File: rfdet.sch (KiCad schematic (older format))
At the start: 6 parts

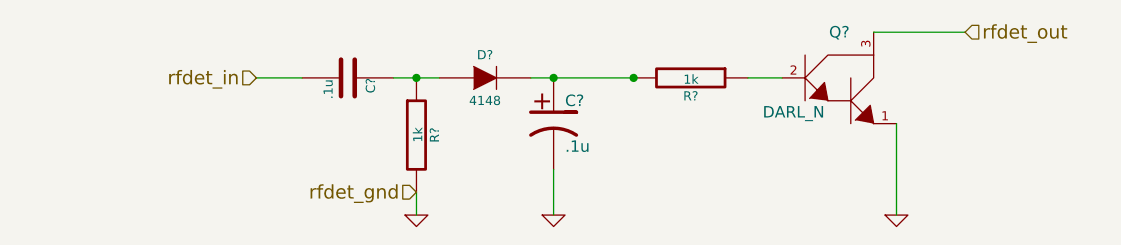
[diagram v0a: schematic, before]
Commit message: Finished/annotated rfdet schematic
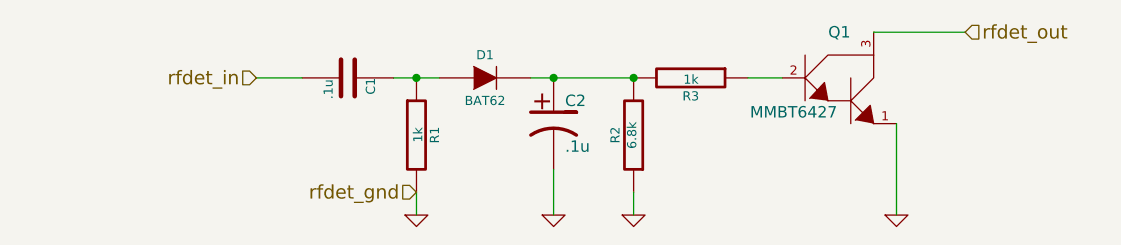
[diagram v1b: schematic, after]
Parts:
- added R2: 6.8k, symbol R
- D1: renamed from D?; value 4148 -> BAT62
- Q1: renamed from Q?; value DARL_N -> MMBT6427
- gave numbers to parts that had none: 4
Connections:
- net GND: now also R2.1
- net at C2.1, D1.2 (K), R3.2: now also R2.2
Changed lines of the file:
@@
 LIBS:contrib
 LIBS:valves
-LIBS:transfo-dots
 LIBS:mcus
+LIBS:transformers
 LIBS:qrpamp-cache
 EELAYER 24 0
@@
 $EndDescr
 $Comp
-L C C?
+L C C1
 U 1 1 5470CFC5
 P 4800 3700
-F 0 "C?" H 4800 3800 40  0000 L CNN
+F 0 "C1" H 4800 3800 40  0000 L CNN
 F 1 ".1u" H 4806 3615 40  0000 L CNN
 F 2 "" H 4838 3550 30  0000 C CNN
@@
 $EndComp
 $Comp
-L DIODE D?
+L DIODE D1
 U 1 1 5470CFD9
 P 5400 3700
-F 0 "D?" H 5400 3800 40  0000 C CNN
-F 1 "4148" H 5400 3600 40  0000 C CNN
+F 0 "D1" H 5400 3800 40  0000 C CNN
+F 1 "BAT62" H 5400 3600 40  0000 C CNN
 F 2 "" H 5400 3700 60  0000 C CNN
 F 3 "" H 5400 3700 60  0000 C CNN
@@
 $EndComp
 $Comp
-L CP1 C?
+L CP1 C2
 U 1 1 5470CFED
 P 5700 3900
-F 0 "C?" H 5750 4000 50  0000 L CNN
+F 0 "C2" H 5750 4000 50  0000 L CNN
 F 1 ".1u" H 5750 3800 50  0000 L CNN
 F 2 "" H 5700 3900 60  0000 C CNN
@@
 $EndComp
 $Comp
-L R R?
+L R R3
 U 1 1 5470D001
 P 6300 3700
-F 0 "R?" V 6380 3700 40  0000 C CNN
+F 0 "R3" V 6380 3700 40  0000 C CNN
 F 1 "1k" V 6307 3701 40  0000 C CNN
 F 2 "" V 6230 3700 30  0000 C CNN
@@
 $EndComp
 $Comp
-L R R?
+L R R1
 U 1 1 5470D02C
 P 5100 3950
-F 0 "R?" V 5180 3950 40  0000 C CNN
+F 0 "R1" V 5180 3950 40  0000 C CNN
 F 1 "1k" V 5107 3951 40  0000 C CNN
 F 2 "" V 5030 3950 30  0000 C CNN
@@
 $EndComp
 $Comp
-L GND #PWR?
+L GND #PWR2
 U 1 1 5470D04B
 P 5700 4300
-F 0 "#PWR?" H 5700 4300 30  0001 C CNN
+F 0 "#PWR2" H 5700 4300 30  0001 C CNN
 F 1 "GND" H 5700 4230 30  0001 C CNN
 F 2 "" H 5700 4300 60  0000 C CNN
@@
 $EndComp
 $Comp
-L GND #PWR?
+L GND #PWR1
 U 1 1 5470D056
 P 5100 4300
-F 0 "#PWR?" H 5100 4300 30  0001 C CNN
+F 0 "#PWR1" H 5100 4300 30  0001 C CNN
 F 1 "GND" H 5100 4230 30  0001 C CNN
 F 2 "" H 5100 4300 60  0000 C CNN
@@
 	4600 3700 4400 3700
 $Comp
-L DARL_N Q?
+L DARL_N Q1
 U 1 1 5470D157
 P 6950 3750
-F 0 "Q?" H 6950 4000 50  0000 C CNN
-F 1 "DARL_N" H 6750 3650 50  0000 C CNN
+F 0 "Q1" H 6950 4000 50  0000 C CNN
+F 1 "MMBT6427" H 6750 3650 50  0000 C CNN
 F 2 "" H 6950 3750 60  0000 C CNN
 F 3 "" H 6950 3750 60  0000 C CNN
@@
 	6550 3700 6700 3700
 $Comp
-L GND #PWR?
+L GND #PWR4
 U 1 1 5470D254
 P 7200 4300
-F 0 "#PWR?" H 7200 4300 30  0001 C CNN
+F 0 "#PWR4" H 7200 4300 30  0001 C CNN
 F 1 "GND" H 7200 4230 30  0001 C CNN
 F 2 "" H 7200 4300 60  0000 C CNN
@@
 Text HLabel 5100 4200 0    60   Input ~ 0
 rfdet_gnd
+$Comp
+L R R2
+U 1 1 5477B801
+P 6050 3950
+F 0 "R2" V 6130 3950 40  0000 C CNN
+F 1 "6.8k" V 6057 3951 40  0000 C CNN
+F 2 "" V 5980 3950 30  0000 C CNN
+F 3 "" H 6050 3950 30  0000 C CNN
+	1    6050 3950
+	-1   0    0    1
+$EndComp
+$Comp
+L GND #PWR3
+U 1 1 5477B80C
+P 6050 4300
+F 0 "#PWR3" H 6050 4300 30  0001 C CNN
+F 1 "GND" H 6050 4230 30  0001 C CNN
+F 2 "" H 6050 4300 60  0000 C CNN
+F 3 "" H 6050 4300 60  0000 C CNN
+	1    6050 4300
+	1    0    0    -1
+$EndComp
+Wire Wire Line
+	6050 4200 6050 4300
 $EndSCHEMATC

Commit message: Added simulation dir
Also, due to simulation, modified the rf detector circuit
to have higher input impdedance to distort the input rf
less.
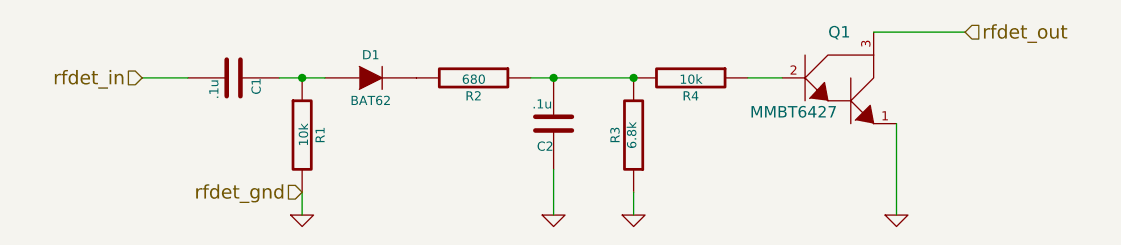
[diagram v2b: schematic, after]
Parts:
- removed C2: .1u, symbol CP1
- added C2: .1u, symbol C
- added R2: 680, symbol R
- R1: value 1k -> 10k
- R4: renamed from R3; value 1k -> 10k
- renumbered R2 to R3
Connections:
- net GND: now also C2.1
- net at R3.2, R4.2: now also C2.2, R2.1; no longer D1.2 (K)
- new net: D1.2 (K), R2.2
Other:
- moved on the sheet: C1, D1, R1
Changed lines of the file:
@@
 L C C1
 U 1 1 5470CFC5
-P 4800 3700
-F 0 "C1" H 4800 3800 40  0000 L CNN
-F 1 ".1u" H 4806 3615 40  0000 L CNN
-F 2 "" H 4838 3550 30  0000 C CNN
-F 3 "" H 4800 3700 60  0000 C CNN
-	1    4800 3700
+P 4300 3700
+F 0 "C1" H 4300 3800 40  0000 L CNN
+F 1 ".1u" H 4306 3615 40  0000 L CNN
+F 2 "" H 4338 3550 30  0000 C CNN
+F 3 "" H 4300 3700 60  0000 C CNN
+	1    4300 3700
 	0    1    1    0
 $EndComp
@@
 L DIODE D1
 U 1 1 5470CFD9
-P 5400 3700
-F 0 "D1" H 5400 3800 40  0000 C CNN
-F 1 "BAT62" H 5400 3600 40  0000 C CNN
-F 2 "" H 5400 3700 60  0000 C CNN
-F 3 "" H 5400 3700 60  0000 C CNN
-	1    5400 3700
+P 4900 3700
+F 0 "D1" H 4900 3800 40  0000 C CNN
+F 1 "BAT62" H 4900 3600 40  0000 C CNN
+F 2 "" H 4900 3700 60  0000 C CNN
+F 3 "" H 4900 3700 60  0000 C CNN
+	1    4900 3700
 	1    0    0    -1
 $EndComp
 $Comp
-L CP1 C2
-U 1 1 5470CFED
-P 5700 3900
-F 0 "C2" H 5750 4000 50  0000 L CNN
-F 1 ".1u" H 5750 3800 50  0000 L CNN
-F 2 "" H 5700 3900 60  0000 C CNN
-F 3 "" H 5700 3900 60  0000 C CNN
-	1    5700 3900
-	1    0    0    -1
-$EndComp
-$Comp
-L R R3
+L R R4
 U 1 1 5470D001
 P 6300 3700
-F 0 "R3" V 6380 3700 40  0000 C CNN
-F 1 "1k" V 6307 3701 40  0000 C CNN
+F 0 "R4" V 6380 3700 40  0000 C CNN
+F 1 "10k" V 6307 3701 40  0000 C CNN
 F 2 "" V 6230 3700 30  0000 C CNN
 F 3 "" H 6300 3700 30  0000 C CNN
@@
 L R R1
 U 1 1 5470D02C
-P 5100 3950
-F 0 "R1" V 5180 3950 40  0000 C CNN
-F 1 "1k" V 5107 3951 40  0000 C CNN
-F 2 "" V 5030 3950 30  0000 C CNN
-F 3 "" H 5100 3950 30  0000 C CNN
-	1    5100 3950
+P 4600 3950
+F 0 "R1" V 4680 3950 40  0000 C CNN
+F 1 "10k" V 4607 3951 40  0000 C CNN
+F 2 "" V 4530 3950 30  0000 C CNN
+F 3 "" H 4600 3950 30  0000 C CNN
+	1    4600 3950
 	1    0    0    -1
 $EndComp
@@
 L GND #PWR1
 U 1 1 5470D056
-P 5100 4300
-F 0 "#PWR1" H 5100 4300 30  0001 C CNN
-F 1 "GND" H 5100 4230 30  0001 C CNN
-F 2 "" H 5100 4300 60  0000 C CNN
-F 3 "" H 5100 4300 60  0000 C CNN
-	1    5100 4300
+P 4600 4300
+F 0 "#PWR1" H 4600 4300 30  0001 C CNN
+F 1 "GND" H 4600 4230 30  0001 C CNN
+F 2 "" H 4600 4300 60  0000 C CNN
+F 3 "" H 4600 4300 60  0000 C CNN
+	1    4600 4300
 	1    0    0    -1
 $EndComp
 Wire Wire Line
-	5000 3700 5200 3700
-Connection ~ 5100 3700
+	4500 3700 4700 3700
+Connection ~ 4600 3700
 Connection ~ 5700 3700
 Connection ~ 6050 3700
@@
 	5700 4100 5700 4300
 Wire Wire Line
-	5100 4200 5100 4300
+	4600 4200 4600 4300
 Wire Wire Line
-	4600 3700 4400 3700
+	4100 3700 3900 3700
 $Comp
 L DARL_N Q1
@@
 Text HLabel 7500 3500 2    60   Input ~ 0
 rfdet_out
-Text HLabel 4400 3700 0    60   Input ~ 0
+Text HLabel 3900 3700 0    60   Input ~ 0
 rfdet_in
-Text HLabel 5100 4200 0    60   Input ~ 0
+Text HLabel 4600 4200 0    60   Input ~ 0
 rfdet_gnd
 $Comp
-L R R2
+L R R3
 U 1 1 5477B801
 P 6050 3950
-F 0 "R2" V 6130 3950 40  0000 C CNN
+F 0 "R3" V 6130 3950 40  0000 C CNN
 F 1 "6.8k" V 6057 3951 40  0000 C CNN
 F 2 "" V 5980 3950 30  0000 C CNN
@@
 Wire Wire Line
 	6050 4200 6050 4300
+$Comp
+L R R2
+U 1 1 54788FD0
+P 5350 3700
+F 0 "R2" V 5430 3700 40  0000 C CNN
+F 1 "680" V 5357 3701 40  0000 C CNN
+F 2 "" V 5280 3700 30  0000 C CNN
+F 3 "" H 5350 3700 30  0000 C CNN
+	1    5350 3700
+	0    1    1    0
+$EndComp
+$Comp
+L C C2
+U 1 1 54788FE2
+P 5700 3900
+F 0 "C2" H 5700 4000 40  0000 L CNN
+F 1 ".1u" H 5706 3815 40  0000 L CNN
+F 2 "" H 5738 3750 30  0000 C CNN
+F 3 "" H 5700 3900 60  0000 C CNN
+	1    5700 3900
+	-1   0    0    1
+$EndComp
 $EndSCHEMATC

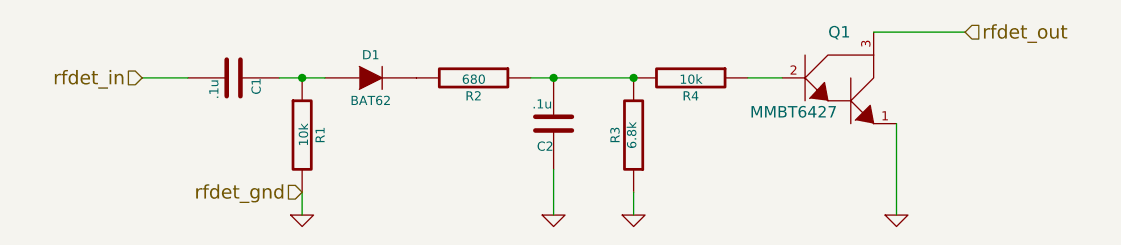
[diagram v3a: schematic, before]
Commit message: Associate more footprints
- Removed flyback diodes from amp
- Changed BAT62 -> SD101 (BAT62 is EOL)
- Changed R and C footprints for hand-soldered versions
- Associated through-hole cap footprints
- Associated regulator footprints
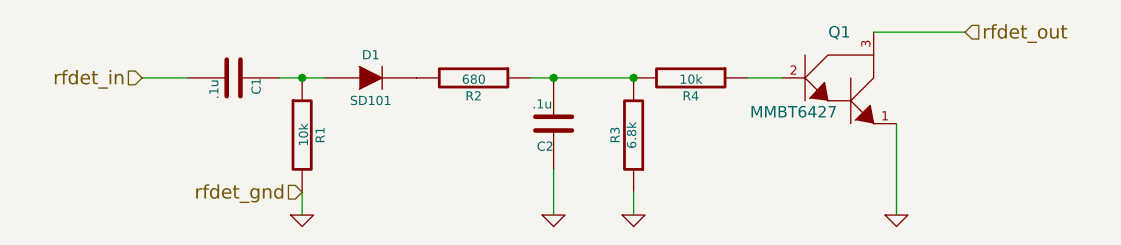
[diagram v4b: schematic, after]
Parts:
- C1, C2: footprint (none) -> Capacitors_SMD:C_0805_HandSoldering
- D1: value BAT62 -> SD101
- R1, R2, R3, R4: footprint (none) -> Resistors_SMD:R_1206_HandSoldering
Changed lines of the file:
@@
 LIBS:transformers
 LIBS:qrpamp-cache
-EELAYER 24 0
+EELAYER 25 0
 EELAYER END
 $Descr A4 11693 8268
@@
 F 0 "C1" H 4300 3800 40  0000 L CNN
 F 1 ".1u" H 4306 3615 40  0000 L CNN
-F 2 "" H 4338 3550 30  0000 C CNN
+F 2 "Capacitors_SMD:C_0805_HandSoldering" H 4338 3550 30  0001 C CNN
 F 3 "" H 4300 3700 60  0000 C CNN
 	1    4300 3700
@@
 P 4900 3700
 F 0 "D1" H 4900 3800 40  0000 C CNN
-F 1 "BAT62" H 4900 3600 40  0000 C CNN
-F 2 "" H 4900 3700 60  0000 C CNN
+F 1 "SD101" H 4900 3600 40  0000 C CNN
+F 2 "" H 4900 3700 60  0001 C CNN
 F 3 "" H 4900 3700 60  0000 C CNN
 	1    4900 3700
@@
 F 0 "R4" V 6380 3700 40  0000 C CNN
 F 1 "10k" V 6307 3701 40  0000 C CNN
-F 2 "" V 6230 3700 30  0000 C CNN
+F 2 "Resistors_SMD:R_1206_HandSoldering" V 6230 3700 30  0001 C CNN
 F 3 "" H 6300 3700 30  0000 C CNN
 	1    6300 3700
@@
 F 0 "R1" V 4680 3950 40  0000 C CNN
 F 1 "10k" V 4607 3951 40  0000 C CNN
-F 2 "" V 4530 3950 30  0000 C CNN
+F 2 "Resistors_SMD:R_1206_HandSoldering" V 4530 3950 30  0001 C CNN
 F 3 "" H 4600 3950 30  0000 C CNN
 	1    4600 3950
@@
 F 0 "Q1" H 6950 4000 50  0000 C CNN
 F 1 "MMBT6427" H 6750 3650 50  0000 C CNN
-F 2 "" H 6950 3750 60  0000 C CNN
+F 2 "" H 6950 3750 60  0001 C CNN
 F 3 "" H 6950 3750 60  0000 C CNN
 	1    6950 3750
@@
 F 0 "R3" V 6130 3950 40  0000 C CNN
 F 1 "6.8k" V 6057 3951 40  0000 C CNN
-F 2 "" V 5980 3950 30  0000 C CNN
+F 2 "Resistors_SMD:R_1206_HandSoldering" V 5980 3950 30  0001 C CNN
 F 3 "" H 6050 3950 30  0000 C CNN
 	1    6050 3950
@@
 F 0 "R2" V 5430 3700 40  0000 C CNN
 F 1 "680" V 5357 3701 40  0000 C CNN
-F 2 "" V 5280 3700 30  0000 C CNN
+F 2 "Resistors_SMD:R_1206_HandSoldering" V 5280 3700 30  0001 C CNN
 F 3 "" H 5350 3700 30  0000 C CNN
 	1    5350 3700
@@
 F 0 "C2" H 5700 4000 40  0000 L CNN
 F 1 ".1u" H 5706 3815 40  0000 L CNN
-F 2 "" H 5738 3750 30  0000 C CNN
+F 2 "Capacitors_SMD:C_0805_HandSoldering" H 5738 3750 30  0001 C CNN
 F 3 "" H 5700 3900 60  0000 C CNN
 	1    5700 3900

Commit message: Finished band filters schematic
- Associated last of the capacitors with footprints
- Associated inductors
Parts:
- D1: footprint (none) -> nu9j-footprints:SOD-123
- Q1: footprint (none) -> Transistors_SMD:sot23
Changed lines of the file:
@@
 F 0 "D1" H 4900 3800 40  0000 C CNN
 F 1 "SD101" H 4900 3600 40  0000 C CNN
-F 2 "" H 4900 3700 60  0001 C CNN
+F 2 "nu9j-footprints:SOD-123" H 4900 3700 60  0001 C CNN
 F 3 "" H 4900 3700 60  0000 C CNN
 	1    4900 3700
@@
 $EndComp
 $Comp
-L GND #PWR17
+L GND #PWR016
 U 1 1 5470D04B
 P 5700 4300
-F 0 "#PWR17" H 5700 4300 30  0001 C CNN
+F 0 "#PWR016" H 5700 4300 30  0001 C CNN
 F 1 "GND" H 5700 4230 30  0001 C CNN
 F 2 "" H 5700 4300 60  0000 C CNN
@@
 $EndComp
 $Comp
-L GND #PWR16
+L GND #PWR017
 U 1 1 5470D056
 P 4600 4300
-F 0 "#PWR16" H 4600 4300 30  0001 C CNN
+F 0 "#PWR017" H 4600 4300 30  0001 C CNN
 F 1 "GND" H 4600 4230 30  0001 C CNN
 F 2 "" H 4600 4300 60  0000 C CNN
@@
 F 0 "Q1" H 6950 4000 50  0000 C CNN
 F 1 "MMBT6427" H 6750 3650 50  0000 C CNN
-F 2 "" H 6950 3750 60  0001 C CNN
+F 2 "Transistors_SMD:sot23" H 6950 3750 60  0001 C CNN
 F 3 "" H 6950 3750 60  0000 C CNN
 	1    6950 3750
@@
 	6550 3700 6700 3700
 $Comp
-L GND #PWR19
+L GND #PWR018
 U 1 1 5470D254
 P 7200 4300
-F 0 "#PWR19" H 7200 4300 30  0001 C CNN
+F 0 "#PWR018" H 7200 4300 30  0001 C CNN
 F 1 "GND" H 7200 4230 30  0001 C CNN
 F 2 "" H 7200 4300 60  0000 C CNN
@@
 $EndComp
 $Comp
-L GND #PWR18
+L GND #PWR019
 U 1 1 5477B80C
 P 6050 4300
-F 0 "#PWR18" H 6050 4300 30  0001 C CNN
+F 0 "#PWR019" H 6050 4300 30  0001 C CNN
 F 1 "GND" H 6050 4230 30  0001 C CNN
 F 2 "" H 6050 4300 60  0000 C CNN
